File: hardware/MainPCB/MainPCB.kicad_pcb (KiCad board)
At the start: 2 copper layers, 100 x 65 mm, 49 parts, among them J1 Conn_01x05, J2 Conn_01x02, J3 Conn_01x03, J4 USB4125-GF-A_REVA2, Q1 TIP120, SW2 SW_Push, U1 ESP32-CAM, U2 RASPBERRY_PI_PICO, U3 LSM6DSO32XTR

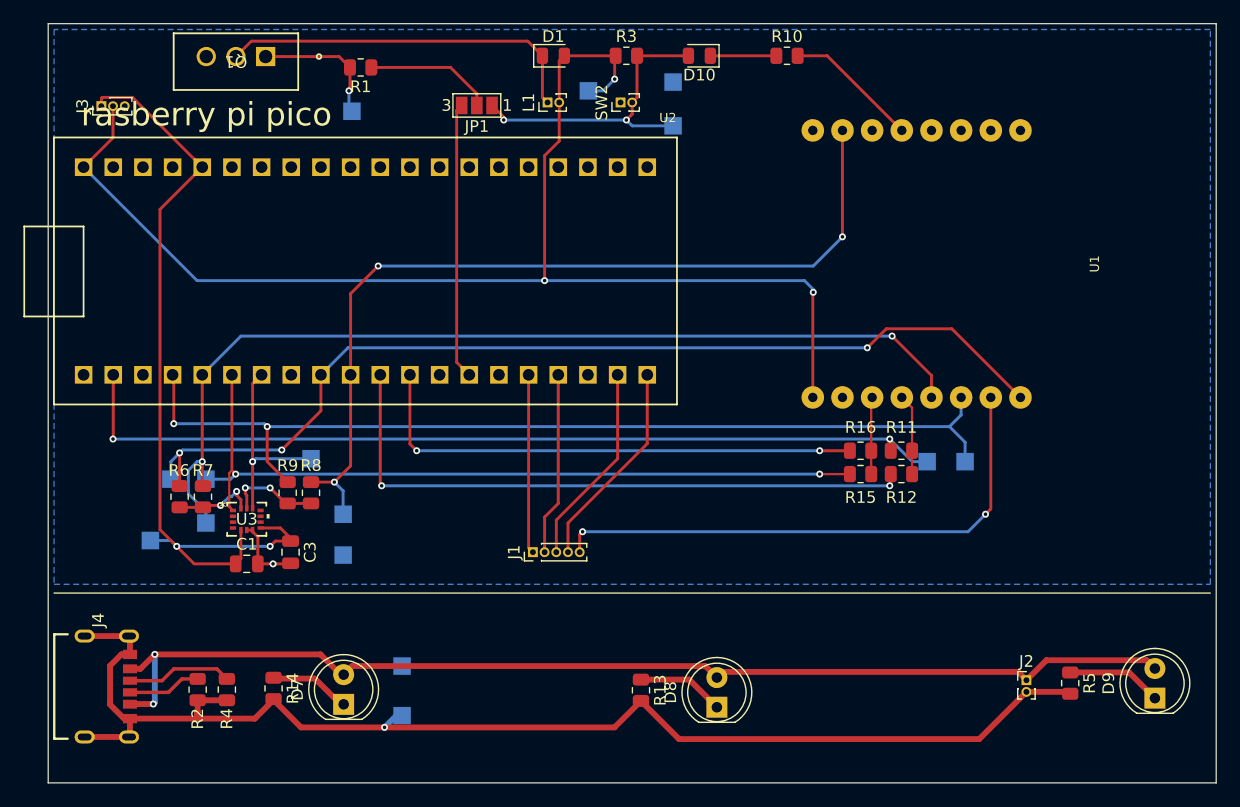
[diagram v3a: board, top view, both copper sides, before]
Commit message: refac: remade the pcb to put the IMU under the PI
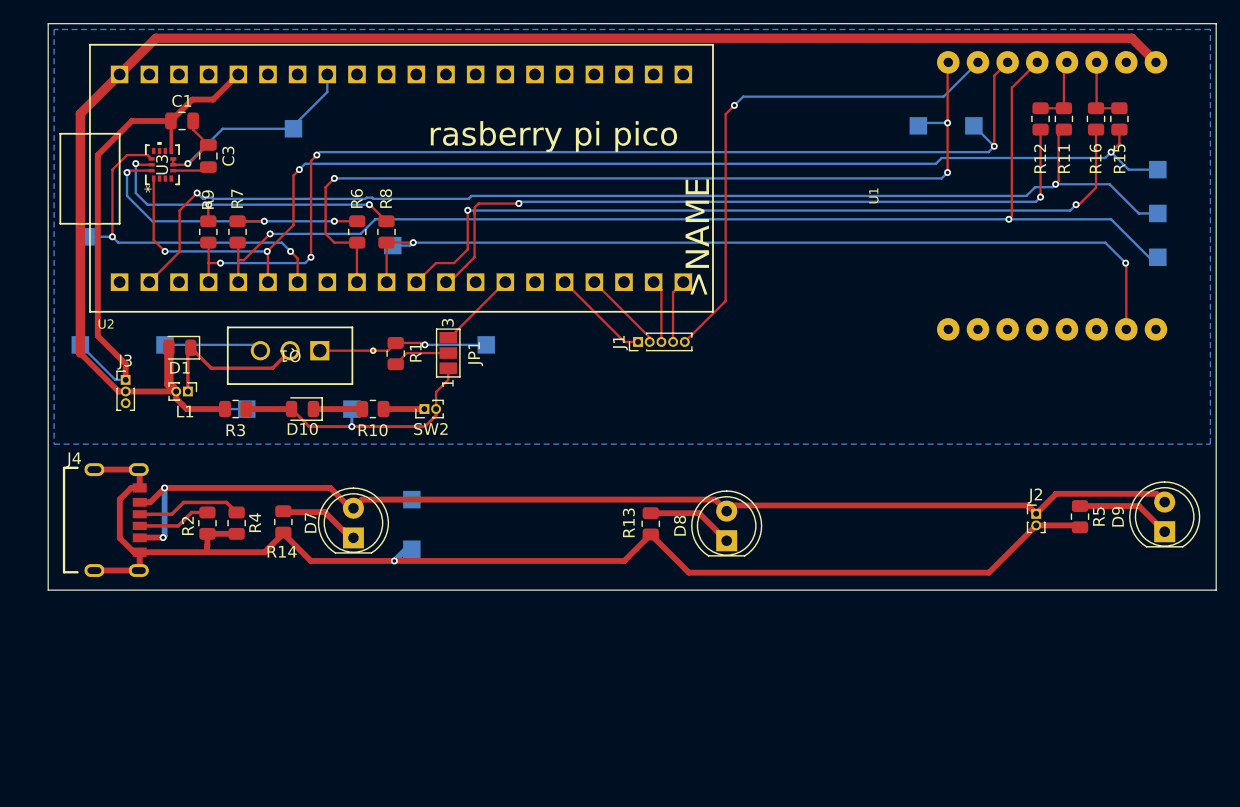
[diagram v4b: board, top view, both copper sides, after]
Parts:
- moved TP4 85.7 mm to (145.0, 62.5)
- moved TP13 84.6 mm to (145.0, 70.0)
- moved TP5 70.8 mm to (124.5, 58.8)
- moved TP3 49.0 mm to (60.0, 77.5)
- moved R10 46.6 mm to (77.8, 83.0)
- moved D10 45.5 mm to (71.8, 83.0)
- moved R3 45.1 mm to (66.0, 83.0)
- moved D1 40.6 mm to (61.3, 77.7), turned to 180 degrees
- moved TP10 40.0 mm to (67.0, 83.0)
- moved L1 39.5 mm to (62.0, 81.5), turned to -90 degrees
- moved C1 38.3 mm to (61.5, 58.3)
- moved R15 37.6 mm to (141.7, 58.2), turned to -90 degrees
- moved TP11 36.7 mm to (71.0, 59.0)
- moved TP14 36.7 mm to (76.0, 83.0)
- moved R16 34.8 mm to (139.7, 58.2), turned to -90 degrees
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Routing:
- net /MISO: track 67.6 -> 103.1 mm, vias 2 -> 4
- net VUSB: track 111.4 -> 141.9 mm, vias 3 -> 0
- net 3V3: track 70.8 -> 45.9 mm, vias 2 -> 0
- net /CS2: track 77.0 -> 98.5 mm
- net Net-(U3-SDA): track 7.23 -> 27.1 mm, vias 2 -> 3
- net Net-(U3-SCL): track 7.98 -> 27.8 mm, vias 2 -> 3
- net /UART RX: track 43.8 -> 62.3 mm
- net Net-(D1-A): track 31.5 -> 13.7 mm
- net /Solenoid: track 23.7 -> 6.86 mm
- net GND: track 18.2 -> 34.9 mm
- net /MOSI: track 83.2 -> 99.4 mm
- net /UART TX: track 54.1 -> 68.5 mm
- net /CS1: track 16.9 -> 30.7 mm, vias 1 -> 2
- net /PI_IO15: track 18.0 -> 5.48 mm
- net /PI_IO14: track 17.6 -> 5.40 mm
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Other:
- board size 100 x 65 mm -> 100 x 48.5 mm

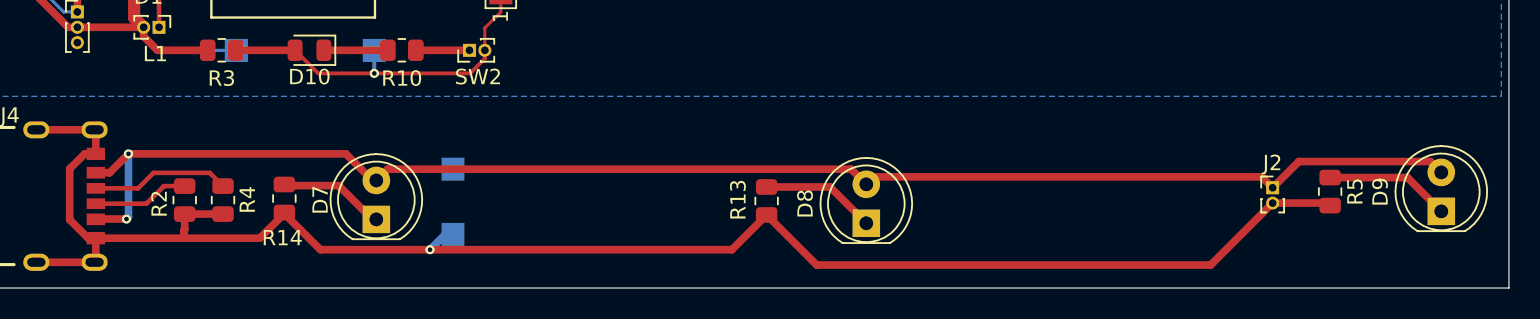
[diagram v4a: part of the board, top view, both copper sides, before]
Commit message: refac: Changed the LEDs to be clumped together. I should stop making the gerber files before Sid checks but idgaf atp
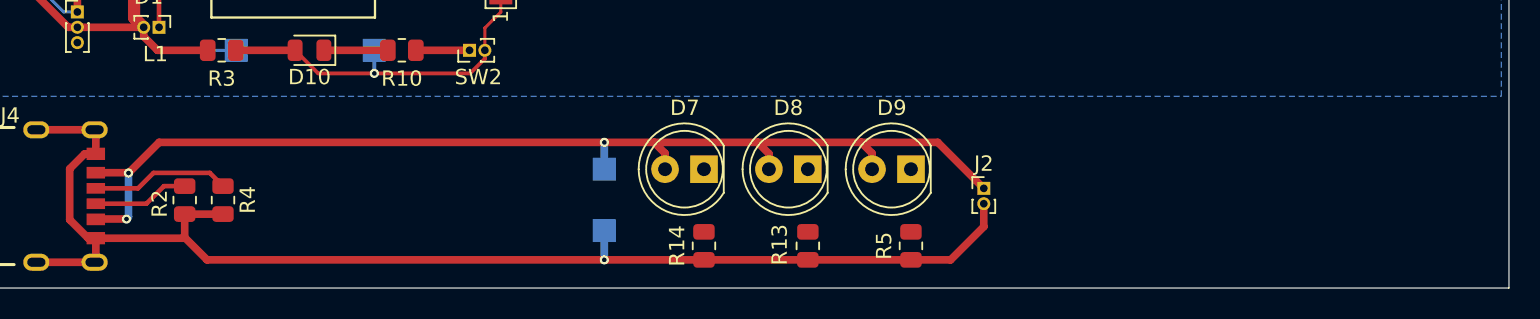
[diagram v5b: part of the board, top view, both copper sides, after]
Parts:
- moved D9 34.7 mm to (111.0, 90.8), turned to 180 degrees
- moved R5 27.6 mm to (111.0, 95.8)
- moved R14 27.5 mm to (97.5, 95.8)
- moved D7 21.6 mm to (97.5, 90.8), turned to 180 degrees
- moved J2 18.8 mm to (115.8, 92.0)
- moved TP16 9.87 mm to (91.0, 94.8)
- moved TP15 9.87 mm to (91.0, 90.8)
- moved D8 5.19 mm to (104.3, 90.8), turned to 180 degrees
- moved R13 3.97 mm to (104.3, 95.8)
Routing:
- net VLED: track 102.9 -> 72.9 mm, vias 2 -> 3
- net GND_LED: track 110.6 -> 85.3 mm
- net Net-(D9-K): track 8.16 -> 0.00 mm
- net Net-(D8-K): track 7.48 -> 0.00 mm
- net Net-(D7-K): track 7.02 -> 0.00 mm

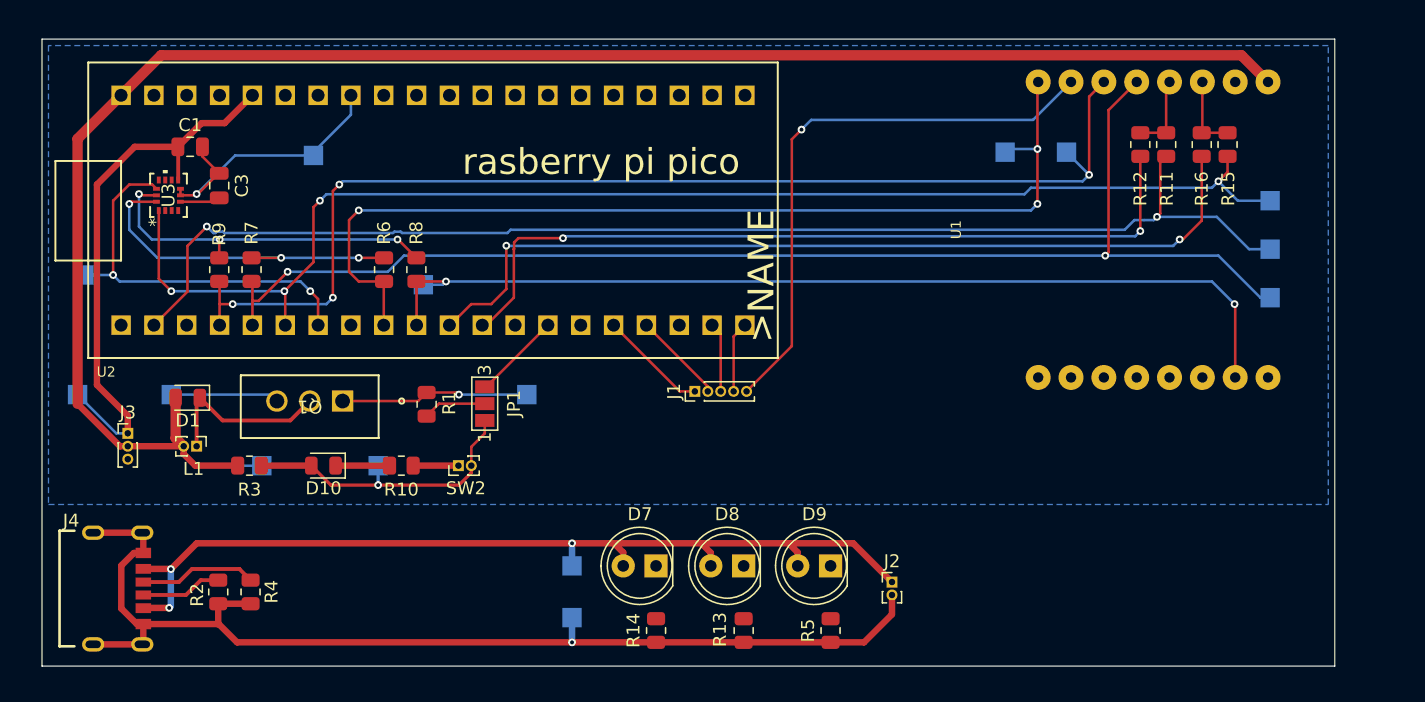
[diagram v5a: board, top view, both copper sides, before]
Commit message: refac: move all wiring done on back to front, add 3d models, gnd plane to led board
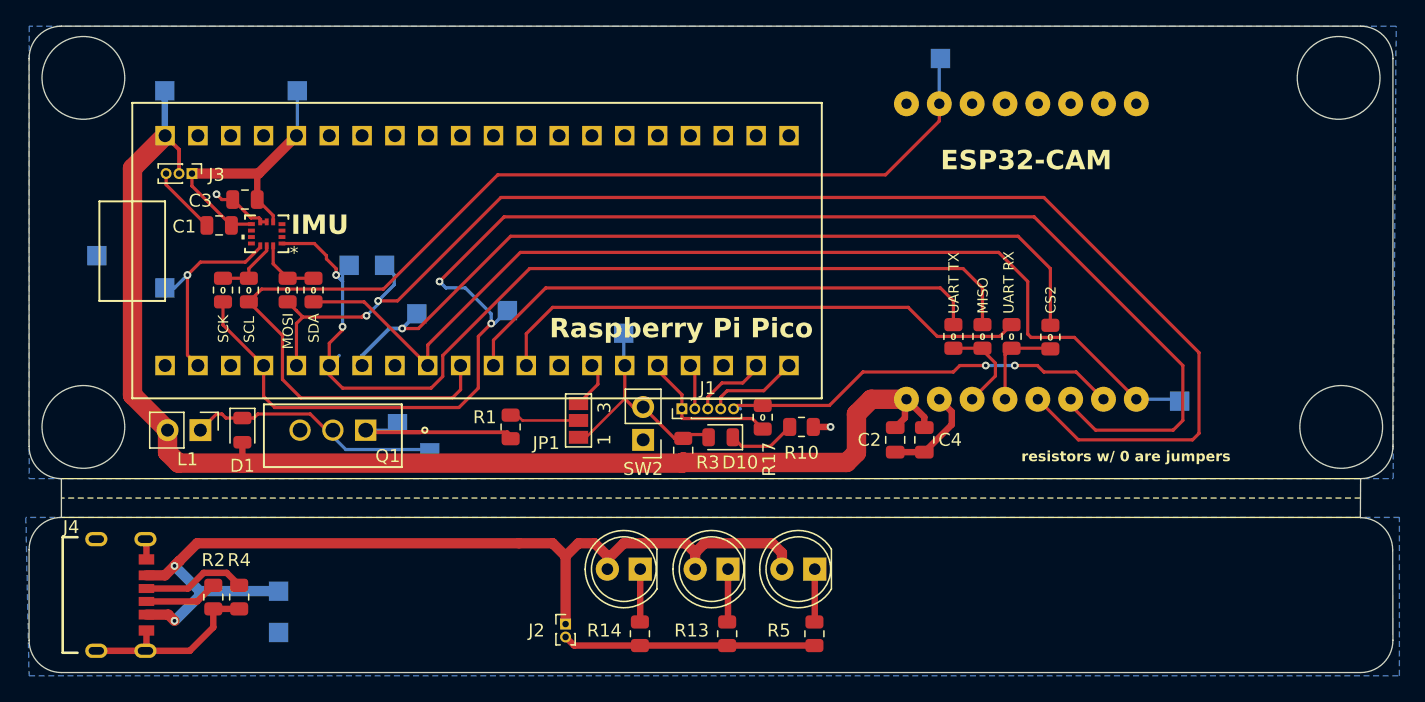
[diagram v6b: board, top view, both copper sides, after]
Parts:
- removed TP3: Transistor_GND_TP, TestPoint:TestPoint_Pad_1.5x1.5mm
- added C2: 10uF, Capacitor_SMD:C_0805_2012Metric, F.Cu at (116.0, 81.0)
- added C4: 0.1uF, Capacitor_SMD:C_0805_2012Metric, F.Cu at (118.2, 81.0)
- added R17: 0, Resistor_SMD:R_0805_2012Metric, F.Cu at (105.8, 79.2)
- added TP17: Transistor_Collector_TP, TestPoint:TestPoint_Pad_1.5x1.5mm, B.Cu at (80.0, 82.0)
- L1, SW2: footprint Connector_PinHeader_1.00mm:PinHeader_1x02_P1.00mm_Vertical -> Connector_PinHeader_2.54mm:PinHeader_1x02_P2.54mm_Vertical
- moved TP4 71.4 mm to (73.8, 67.5)
- moved TP13 68.5 mm to (76.5, 67.5)
- moved TP8 66.2 mm to (79.0, 71.2)
- moved TP9 45.0 mm to (86.0, 71.0)
- moved TP6 43.7 mm to (119.5, 51.5)
- moved R3 33.6 mm to (99.6, 81.8), turned to 90 degrees
- moved R10 31.1 mm to (108.8, 80.0)
- moved D10 30.8 mm to (102.5, 80.8)
- moved TP10 30.0 mm to (59.5, 54.0)
- moved TP12 29.0 mm to (69.8, 54.0)
- moved J2 25.5 mm to (90.5, 95.2)
- moved R16 24.3 mm to (120.5, 73.0), turned to 90 degrees
- moved R15 24.1 mm to (122.8, 73.0), turned to 90 degrees
- moved TP5 23.5 mm to (138.0, 78.0)
- moved TP15 22.8 mm to (68.3, 92.7)
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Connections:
- U2 pad GP1: /CS2 -> /CS1
- U2 pad GP11: unconnected-(U2-PadGP11) -> /Switch
- U2 pad GP5: /CS1 -> /CS2
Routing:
- net GND_LED: track 85.3 -> 36.1 mm, vias 1 -> 0
- net VUSB: track 141.9 -> 101.8 mm
- net /CS2: track 98.5 -> 64.9 mm, vias 2 -> 1
- net /SCK: track 90.4 -> 117.9 mm, vias 4 -> 2
- net /MISO: track 103.1 -> 75.7 mm, vias 4 -> 2
- net /UART TX: track 68.5 -> 41.5 mm, vias 2 -> 0
- net Net-(U3-SCL): track 27.8 -> 5.08 mm, vias 3 -> 0
- net Net-(U3-SDA): track 27.1 -> 4.97 mm, vias 3 -> 0
- net 3V3: track 45.9 -> 23.9 mm
- net /UART RX: track 62.3 -> 42.2 mm, vias 2 -> 0
- net GND: track 34.9 -> 19.2 mm, vias 1 -> 2
- net /CS1: track 30.7 -> 16.1 mm, vias 2 -> 1
- net /CAM_IO2: track 44.4 -> 31.1 mm, vias 1 -> 2
- net /SCL: track 75.0 -> 87.7 mm, vias 2 -> 0
- net /MOSI: track 99.4 -> 107.7 mm
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- added copper zone on B.Cu, net GND_LED
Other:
- board size 100 x 48.5 mm -> 105.5 x 50 mm
- board text added: "0"
- board text added: "3V3 (VDD)"
- board text added: "Base"
- board text added: "CS1"
- board text added: "CS2"
- board text added: "Collector"
- board text added: "ESP32-CAM"
- board text added: "GND"
- board text added: "GND_LED"
- board text added: "IMU"
- board text added: "MISO"
- board text added: "MOSI"
- board text added: "Raspberry Pi Pico"
- board text added: "SCK"
- board text added: "SCL"
- board text added: "SDA"
- board text added: "Switch"
- board text added: "UART RX"
- board text added: "UART TX"
- board text added: "VLED"
- board text added: "VUSB"
- board text added: "resistors w/ 0 are jumpers"

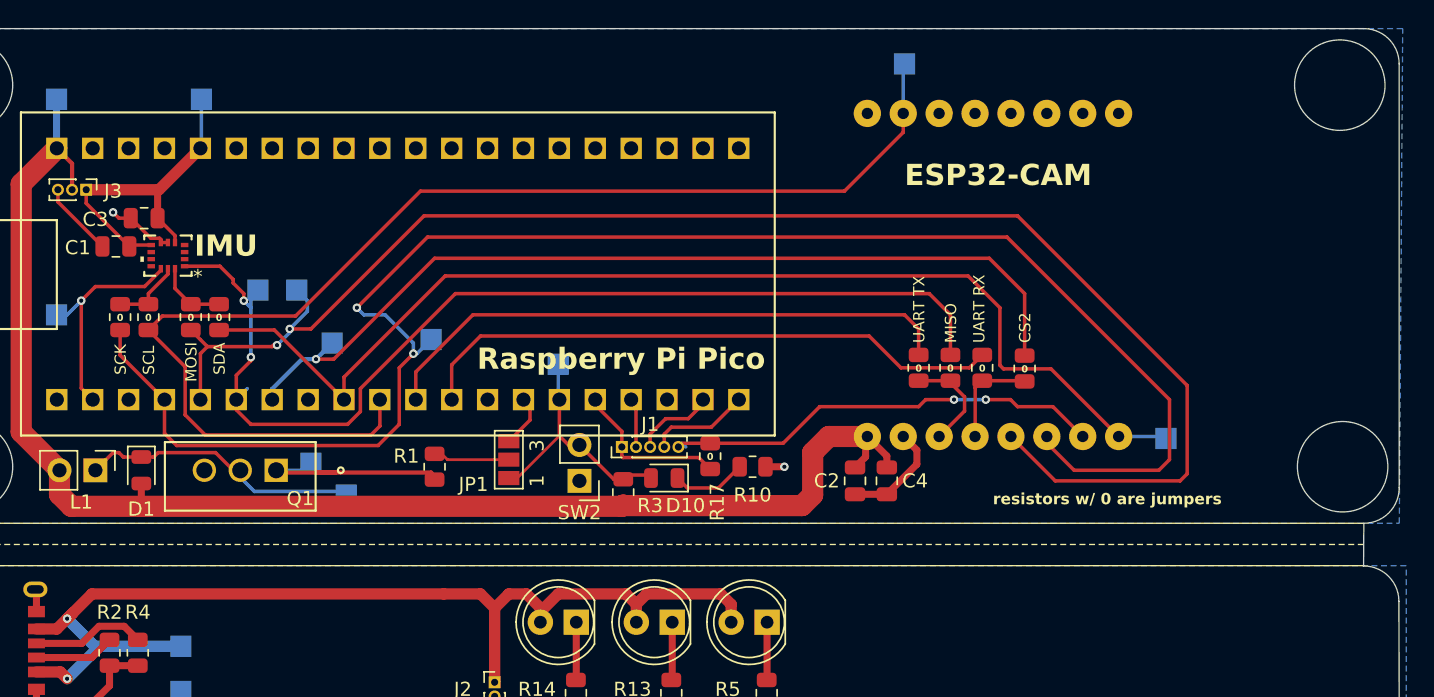
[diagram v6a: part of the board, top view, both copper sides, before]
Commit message: feat: image and via stiching
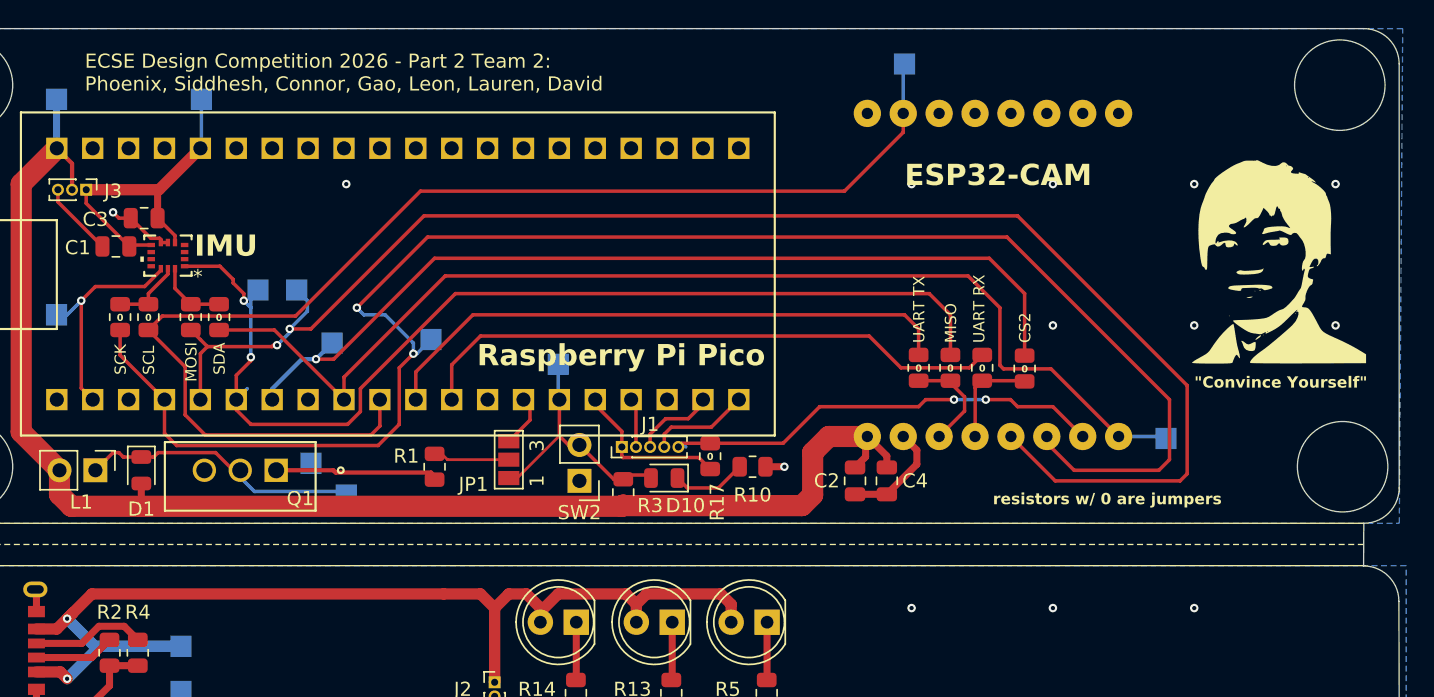
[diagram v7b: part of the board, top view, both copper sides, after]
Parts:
- added G***: LOGO, LOGO, F.Cu at (144.8, 65.5)
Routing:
- net Net-(Q1-Pad1): track 15.6 -> 14.5 mm
- net GND_LED: vias 0 -> 3
- net GND: vias 2 -> 10
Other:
- board text added: "ECSE Design Competition 2026 - Part 2 Team 2: Phoenix, Siddhesh, Connor, Gao, Leon, Lauren, David"
- board text added: "{ "ViaStitching": "0.2", "stitch_zone_0": { "HSpacing": "1", "VSpacing": "1", "HOffset": "0", "VOffset": "0", "Clearance": "0", "Randomize": false } }"
- board text added: "{ "ViaStitching": "0.2", "stitch_zone_0": { "HSpacing": "10", "VSpacing": "10", "HOffset": "0", "VOffset": "0", "Clearance": "0.5", "Randomize": false } }"
- board text added: "{ "ViaStitching": "0.2", "stitch_zone_0": { "HSpacing": "10", "VSpacing": "10", "HOffset": "0", "VOffset": "0", "Clearance": "1", "Randomize": false } }"
- board text added: "{ "ViaStitching": "0.2", "stitch_zone_0": { "HSpacing": "10", "VSpacing": "10", "HOffset": "0", "VOffset": "0", "Clearance": "2", "Randomize": false } }"
- board text added: "{ "ViaStitching": "0.2", "stitch_zone_0": { "HSpacing": "5", "VSpacing": "5", "HOffset": "0", "VOffset": "0", "Clearance": "1", "Randomize": false } }"
- board text added: "{ "ViaStitching": "0.2", "stitch_zone_0": { "HSpacing": "5", "VSpacing": "5", "HOffset": "0", "VOffset": "0", "Clearance": "1", "Randomize": true } }"
- board text added: "{ "ViaStitching": "0.2", "stitch_zone_0": { "HSpacing": "5", "VSpacing": "5", "HOffset": "0", "VOffset": "0", "Clearance": "1.5", "Randomize": false } }"
- board text added: "{dblquote}Convince Yourself{dblquote}"
